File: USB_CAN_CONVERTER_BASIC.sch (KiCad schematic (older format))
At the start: 22 parts, among them P1 CONN_01X04, P2 CONN_01X02, P3 USB_A, P4 CONN_01X04, U1 STM32F042C6Ux, U2 PSD2CAN, U3 SN65HVD232D, U4 MCP1700T-3302E/TT, U5 USBLC6-2

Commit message: USB and CAN connector fix
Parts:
- P3: footprint Connect:USB_A -> usb_ccb_custom:USB_A_DS1097R
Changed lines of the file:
@@
 F 0 "P3" V 10823 4444 50  0000 L CNN
 F 1 "USB_A" V 10868 4444 50  0001 L CNN
-F 2 "Connect:USB_A" V 10750 4150 50  0001 C CNN
+F 2 "usb_ccb_custom:USB_A_DS1097R" V 10750 4150 50  0001 C CNN
 F 3 "" V 10750 4150 50  0000 C CNN
 	1    10800 4250

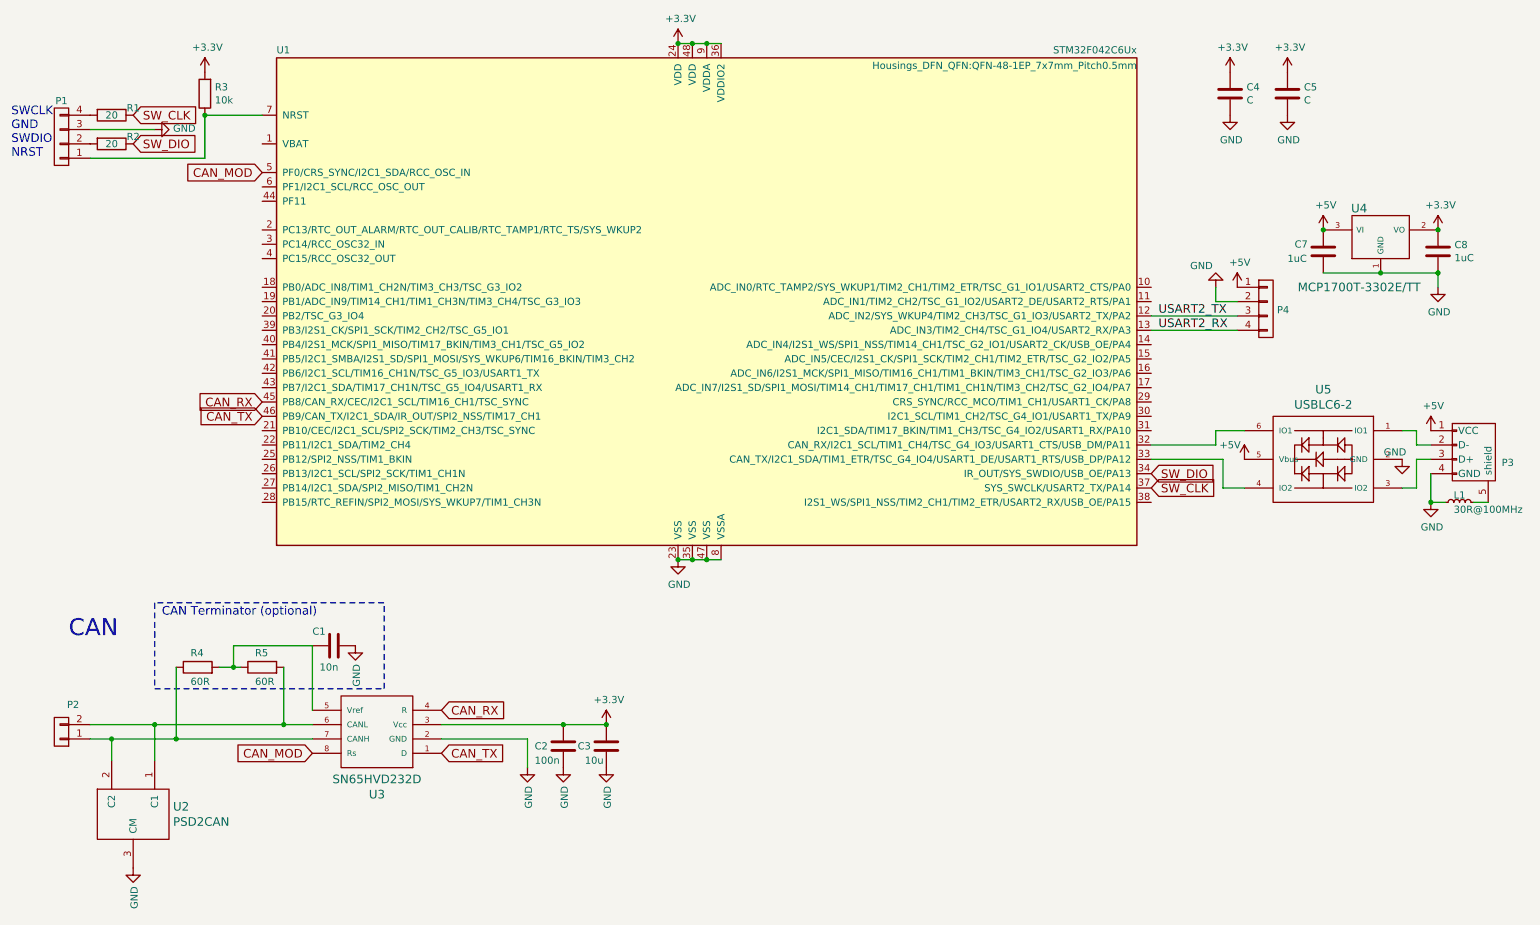
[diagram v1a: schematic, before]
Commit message: UART1 switch, logo creation, CAN footprint update, botom layer replacement.
UART1 switch, logo creation, CAN footprint update, botom layer
replacement.
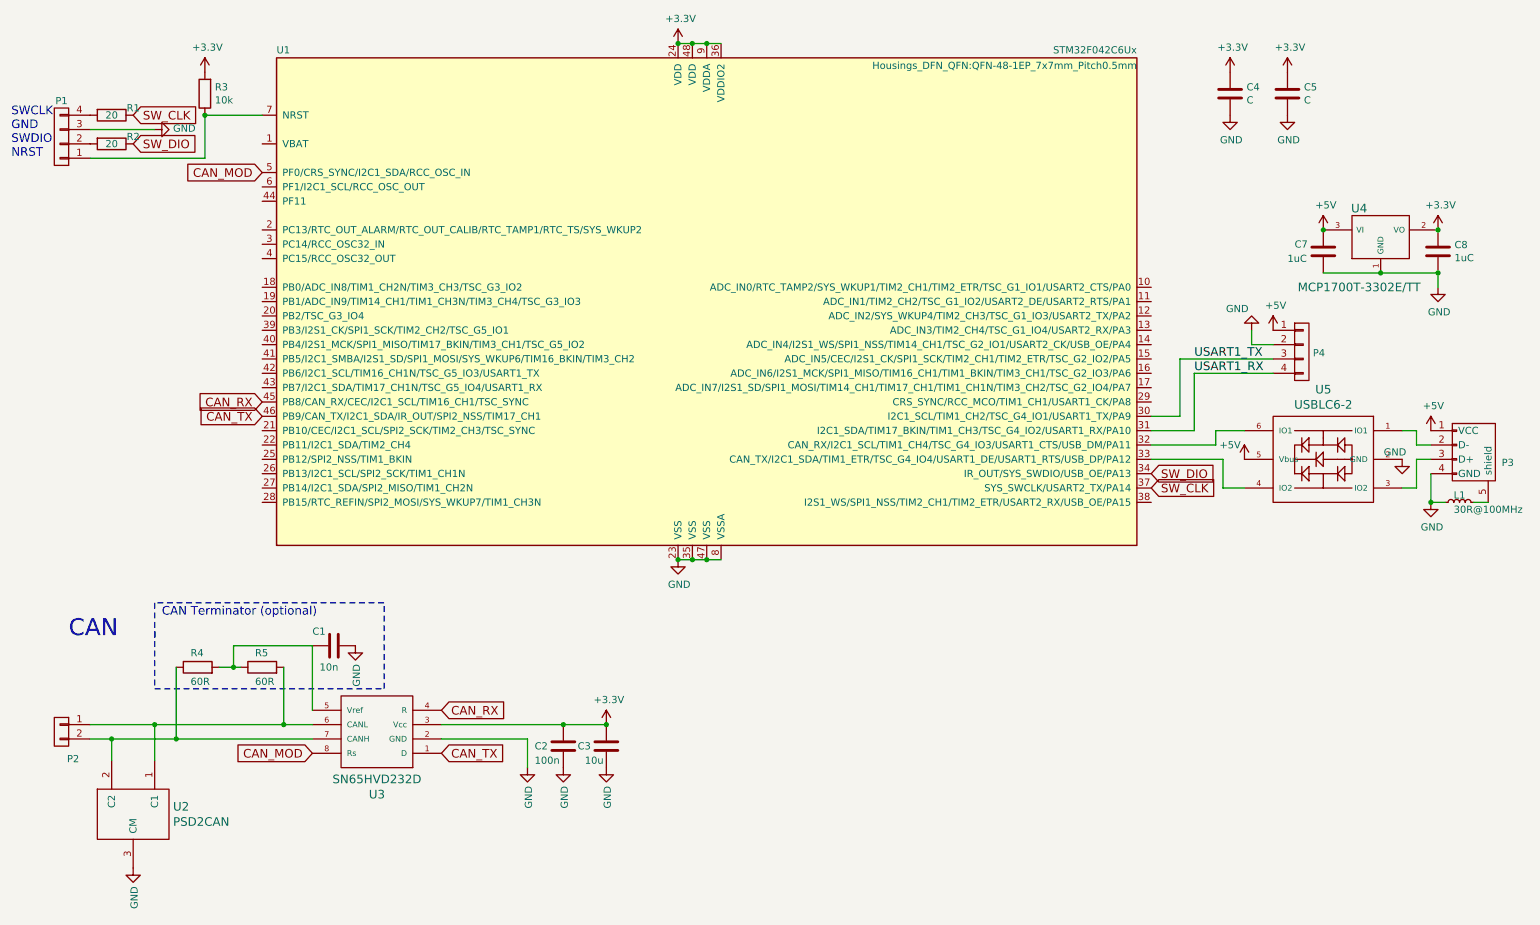
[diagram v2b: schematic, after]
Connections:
- net USART1_TX: now reaches U1.30 (I2C1_SCL/TIM1_CH2/TSC_G4_IO1/USART1_TX/PA9)
- net USART1_TX: now also P4.3 (P3)
- net USART1_RX: now reaches U1.31 (I2C1_SDA/TIM17_BKIN/TIM1_CH3/TSC_G4_IO2/USART1_RX/PA10)
- net USART1_RX: now also P4.4 (P4)
- net at R4.1, U2.2 (C2), U3.7 (CANH): now also P2.2 (P2); no longer P2.1 (P1)
- net at R5.2, U2.1 (C1), U3.6 (CANL): now also P2.1 (P1); no longer P2.2 (P2)
- net USART2_RX: no longer names the net of U1.13 (ADC_IN3/TIM2_CH4/TSC_G1_IO4/USART2_RX/PA3)
- net USART2_RX: no longer P4.4 (P4)
- net USART2_TX: no longer names the net of U1.12 (ADC_IN2/SYS_WKUP4/TIM2_CH3/TSC_G1_IO3/USART2_TX/PA2)
- net USART2_TX: no longer P4.3 (P3)
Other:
- moved on the sheet: P4
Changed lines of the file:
@@
 F 3 "" H 950 6150 50  0000 C CNN
 	1    950  6150
-	-1   0    0    1
+	-1   0    0    -1
 $EndComp
 $Comp
@@
 Wire Wire Line
 	10500 4550 10600 4550
-Wire Wire Line
-	8550 3250 9150 3250
-Wire Wire Line
-	8550 3350 9150 3350
 $Comp
 L GND #PWR022
 U 1 1 571ACD79
-P 9000 3050
-F 0 "#PWR022" H 9000 2800 50  0001 C CNN
-F 1 "GND" H 9100 2900 50  0000 C CNN
-F 2 "" H 9000 3050 50  0000 C CNN
-F 3 "" H 9000 3050 50  0000 C CNN
-	1    9000 3050
+P 9250 3350
+F 0 "#PWR022" H 9250 3100 50  0001 C CNN
+F 1 "GND" H 9350 3200 50  0000 C CNN
+F 2 "" H 9250 3350 50  0000 C CNN
+F 3 "" H 9250 3350 50  0000 C CNN
+	1    9250 3350
 	-1   0    0    1
 $EndComp
@@
 L CONN_01X04 P4
 U 1 1 571E76C6
-P 9350 3200
-F 0 "P4" H 9427 3192 50  0000 L CNN
-F 1 "CONN_01X04" H 9428 3147 50  0001 L CNN
-F 2 "Pin_Headers:Pin_Header_Angled_1x04" H 9427 3147 50  0001 L CNN
-F 3 "" H 9350 3200 50  0000 C CNN
-	1    9350 3200
+P 9600 3500
+F 0 "P4" H 9677 3492 50  0000 L CNN
+F 1 "CONN_01X04" H 9678 3447 50  0001 L CNN
+F 2 "Pin_Headers:Pin_Header_Angled_1x04" H 9677 3447 50  0001 L CNN
+F 3 "" H 9600 3500 50  0000 C CNN
+	1    9600 3500
 	1    0    0    -1
 $EndComp
@@
 L +5V #PWR023
 U 1 1 571E7816
-P 9150 3050
-F 0 "#PWR023" H 9150 2900 50  0001 C CNN
-F 1 "+5V" H 9168 3223 50  0000 C CNN
-F 2 "" H 9150 3050 50  0000 C CNN
-F 3 "" H 9150 3050 50  0000 C CNN
-	1    9150 3050
-	1    0    0    -1
-$EndComp
-Text Label 8600 3250 0    60   ~ 0
-USART2_TX
-Wire Wire Line
-	9000 3150 9150 3150
-Wire Wire Line
-	9000 3150 9000 3050
-Text Label 8600 3350 0    60   ~ 0
-USART2_RX
+P 9400 3350
+F 0 "#PWR023" H 9400 3200 50  0001 C CNN
+F 1 "+5V" H 9418 3523 50  0000 C CNN
+F 2 "" H 9400 3350 50  0000 C CNN
+F 3 "" H 9400 3350 50  0000 C CNN
+	1    9400 3350
+	1    0    0    -1
+$EndComp
+Text Label 8850 3550 0    60   ~ 0
+USART1_TX
+Wire Wire Line
+	9250 3450 9400 3450
+Wire Wire Line
+	9250 3450 9250 3350
+Text Label 8850 3650 0    60   ~ 0
+USART1_RX
 Connection ~ 1950 1850
+Wire Wire Line
+	8850 3650 9400 3650
+Wire Wire Line
+	8550 3950 8750 3950
+Wire Wire Line
+	8750 3950 8750 3550
+Wire Wire Line
+	8750 3550 9400 3550
+Wire Wire Line
+	8550 4050 8850 4050
+Wire Wire Line
+	8850 4050 8850 3650
 $EndSCHEMATC

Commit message: SWD connector update, logo generation,  board otline update.
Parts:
- removed P1: CONN_01X04, Pin_Headers:Pin_Header_Angled_1x04, symbol CONN_01X04
- removed R1, R2: 20, Resistors_SMD:R_0805, symbol R
- added P1: CONN_01X05, usb_ccb_custom:swd_smd_conn5, symbol CONN_01X05
- P4: footprint Pin_Headers:Pin_Header_Angled_1x04 -> usb_ccb_custom:Pin_Header_Angled_1x04m
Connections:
- net +3V3: now also P1.1 (P1)
- net GND: now also P1.4 (P4)
- net SW_CLK: now also P1.3 (P3)
- net SW_DIO: now also P1.5 (P5)
- net at R3.1, U1.7 (NRST): now also P1.2 (P2)
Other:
- note added: "SWCLK\nGND\nSWDIO\nNRST\nVTRG"
- note removed: "SWCLK\nGND\nSWDIO\nNRST"
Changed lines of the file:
@@
-$EndComp
-$Comp
-L CONN_01X04 P1
-U 1 1 570565AB
-P 950 2000
-F 0 "P1" H 950 1750 50  0000 C CNN
-F 1 "CONN_01X04" H 1050 1750 50  0001 C CNN
-F 2 "Pin_Headers:Pin_Header_Angled_1x04" H 950 2000 50  0001 C CNN
-F 3 "" H 950 2000 50  0000 C CNN
-	1    950  2000
-	-1   0    0    1
 $EndComp
 $Comp
@@
 	-1   0    0    1
 $EndComp
-$Comp
-L R R1
-U 1 1 5705681D
-P 1300 1850
-F 0 "R1" V 1250 2000 50  0000 C CNN
-F 1 "20" V 1300 1850 50  0000 C CNN
-F 2 "Resistors_SMD:R_0805" V 1230 1850 50  0001 C CNN
-F 3 "" H 1300 1850 50  0000 C CNN
-	1    1300 1850
-	0    1    1    0
-$EndComp
-$Comp
-L R R2
-U 1 1 570568EE
-P 1300 2050
-F 0 "R2" V 1250 2200 50  0000 C CNN
-F 1 "20" V 1300 2050 50  0000 C CNN
-F 2 "Resistors_SMD:R_0805" V 1230 2050 50  0001 C CNN
-F 3 "" H 1300 2050 50  0000 C CNN
-	1    1300 2050
-	0    1    1    0
-$EndComp
-Text Notes 600  2150 0    60   ~ 0
-SWCLK\nGND\nSWDIO\nNRST
+Text Notes 600  2300 0    60   ~ 0
+SWCLK\nGND\nSWDIO\nNRST\nVTRG
 $Comp
 L GND #PWR02
@@
 Text Notes 1650 5350 0    60   ~ 0
 CAN Terminator (optional)
-Text GLabel 1450 1850 2    60   Input ~ 0
+Text GLabel 1450 2050 2    60   Input ~ 0
 SW_CLK
 Text GLabel 8550 4450 2    60   Input ~ 0
 SW_CLK
-Text GLabel 1450 2050 2    60   Input ~ 0
+Text GLabel 1450 1850 2    60   Input ~ 0
 SW_DIO
 Text GLabel 8550 4350 2    60   Input ~ 0
@@
 F 0 "P4" H 9677 3492 50  0000 L CNN
 F 1 "CONN_01X04" H 9678 3447 50  0001 L CNN
-F 2 "Pin_Headers:Pin_Header_Angled_1x04" H 9677 3447 50  0001 L CNN
+F 2 "usb_ccb_custom:Pin_Header_Angled_1x04m" H 9677 3447 50  0001 L CNN
 F 3 "" H 9600 3500 50  0000 C CNN
 	1    9600 3500
@@
 Wire Wire Line
 	8850 4050 8850 3650
+$Comp
+L CONN_01X05 P1
+U 1 1 57800591
+P 950 2050
+F 0 "P1" H 869 1711 50  0000 C CNN
+F 1 "CONN_01X05" H 869 1710 50  0001 C CNN
+F 2 "usb_ccb_custom:swd_smd_conn5" H 869 1711 50  0001 C CNN
+F 3 "" H 950 2050 50  0000 C CNN
+	1    950  2050
+	-1   0    0    1
+$EndComp
+$Comp
+L +3.3V #PWR024
+U 1 1 57800AA2
+P 1150 2250
+F 0 "#PWR024" H 1150 2100 50  0001 C CNN
+F 1 "+3.3V" H 1168 2423 50  0000 C CNN
+F 2 "" H 1150 2250 50  0000 C CNN
+F 3 "" H 1150 2250 50  0000 C CNN
+	1    1150 2250
+	0    1    1    0
+$EndComp
+Wire Wire Line
+	1150 2050 1450 2050
+Wire Wire Line
+	1450 1850 1150 1850
+Connection ~ 2700 5550
 $EndSCHEMATC

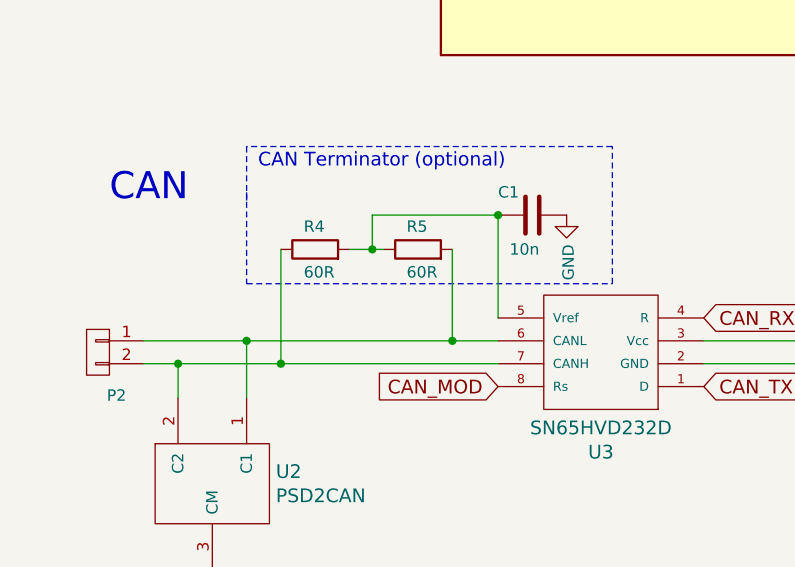
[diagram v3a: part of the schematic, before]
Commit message: CAN Jumpers addition
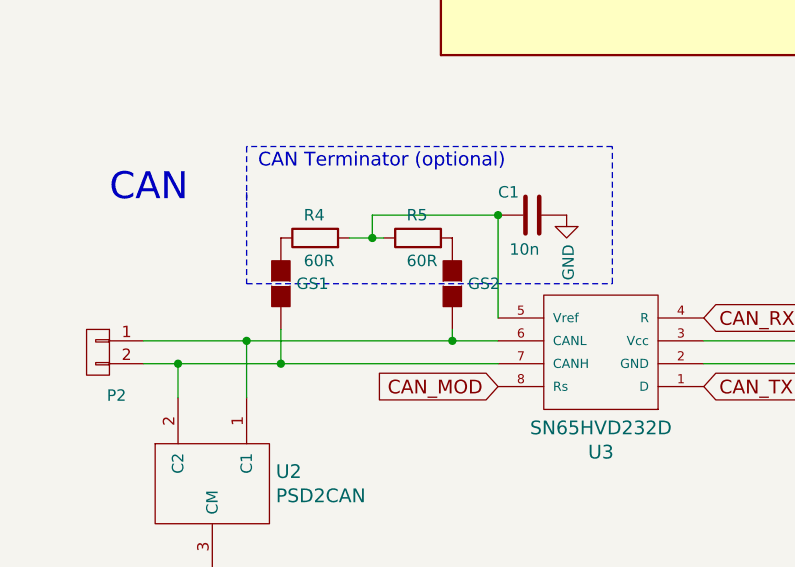
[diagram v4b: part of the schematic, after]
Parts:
- added GS1, GS2: GS2, Connect:GS2, symbol GS2
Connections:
- net at P2.1 (P1), U2.1 (C1), U3.6 (CANL): now also GS2.2 (G2); no longer R5.2
- net at P2.2 (P2), U2.2 (C2), U3.7 (CANH): now also GS1.2 (G2); no longer R4.1
- new net: GS1.1 (G1), R4.1
- new net: GS2.1 (G1), R5.2
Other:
- moved on the sheet: R4, R5
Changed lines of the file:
@@
 $EndComp
 $Comp
-L GND #PWR01
+L GND #PWR11
 U 1 1 570561B2
 P 5250 4950
-F 0 "#PWR01" H 5250 4700 50  0001 C CNN
+F 0 "#PWR11" H 5250 4700 50  0001 C CNN
 F 1 "GND" H 5258 4777 50  0000 C CNN
 F 2 "" H 5250 4950 50  0000 C CNN
@@
 SWCLK\nGND\nSWDIO\nNRST\nVTRG
 $Comp
-L GND #PWR02
+L GND #PWR3
 U 1 1 57056C83
 P 1600 1950
-F 0 "#PWR02" H 1600 1700 50  0001 C CNN
+F 0 "#PWR3" H 1600 1700 50  0001 C CNN
 F 1 "GND" V 1608 1822 50  0000 R CNN
 F 2 "" H 1600 1950 50  0000 C CNN
@@
 $EndComp
 $Comp
-L GND #PWR03
+L GND #PWR22
 U 1 1 5706C070
 P 10500 4550
-F 0 "#PWR03" H 10500 4300 50  0001 C CNN
+F 0 "#PWR22" H 10500 4300 50  0001 C CNN
 F 1 "GND" H 10508 4377 50  0000 C CNN
 F 2 "" H 10500 4550 50  0000 C CNN
@@
 $EndComp
 $Comp
-L +5V #PWR04
+L +5V #PWR21
 U 1 1 5706C74A
 P 10500 4050
-F 0 "#PWR04" H 10500 3900 50  0001 C CNN
+F 0 "#PWR21" H 10500 3900 50  0001 C CNN
 F 1 "+5V" H 10518 4223 50  0000 C CNN
 F 2 "" H 10500 4050 50  0000 C CNN
@@
 $EndComp
 $Comp
-L +5V #PWR05
+L +5V #PWR19
 U 1 1 5706E498
 P 9750 2650
-F 0 "#PWR05" H 9750 2500 50  0001 C CNN
+F 0 "#PWR19" H 9750 2500 50  0001 C CNN
 F 1 "+5V" H 9768 2823 50  0000 C CNN
 F 2 "" H 9750 2650 50  0000 C CNN
@@
 $EndComp
 $Comp
-L +3.3V #PWR06
+L +3.3V #PWR4
 U 1 1 5706E500
 P 1950 1550
-F 0 "#PWR06" H 1950 1400 50  0001 C CNN
+F 0 "#PWR4" H 1950 1400 50  0001 C CNN
 F 1 "+3.3V" H 1968 1723 50  0000 C CNN
 F 2 "" H 1950 1550 50  0000 C CNN
@@
 $EndComp
 $Comp
-L +3.3V #PWR07
+L +3.3V #PWR10
 U 1 1 5706E57B
 P 5250 1350
-F 0 "#PWR07" H 5250 1200 50  0001 C CNN
+F 0 "#PWR10" H 5250 1200 50  0001 C CNN
 F 1 "+3.3V" H 5268 1523 50  0000 C CNN
 F 2 "" H 5250 1350 50  0000 C CNN
@@
 $EndComp
 $Comp
-L +3.3V #PWR08
+L +3.3V #PWR23
 U 1 1 5706E6F4
 P 10550 2650
-F 0 "#PWR08" H 10550 2500 50  0001 C CNN
+F 0 "#PWR23" H 10550 2500 50  0001 C CNN
 F 1 "+3.3V" H 10568 2823 50  0000 C CNN
 F 2 "" H 10550 2650 50  0000 C CNN
@@
 $EndComp
 $Comp
-L GND #PWR09
+L GND #PWR13
 U 1 1 5706EDB2
 P 9100 1850
-F 0 "#PWR09" H 9100 1600 50  0001 C CNN
+F 0 "#PWR13" H 9100 1600 50  0001 C CNN
 F 1 "GND" H 9108 1677 50  0000 C CNN
 F 2 "" H 9100 1850 50  0000 C CNN
@@
 $EndComp
 $Comp
-L GND #PWR010
+L GND #PWR18
 U 1 1 5706EDDA
 P 9500 1850
-F 0 "#PWR010" H 9500 1600 50  0001 C CNN
+F 0 "#PWR18" H 9500 1600 50  0001 C CNN
 F 1 "GND" H 9508 1677 50  0000 C CNN
 F 2 "" H 9500 1850 50  0000 C CNN
@@
 $EndComp
 $Comp
-L +3.3V #PWR011
+L +3.3V #PWR17
 U 1 1 5706EE52
 P 9500 1550
-F 0 "#PWR011" H 9500 1400 50  0001 C CNN
+F 0 "#PWR17" H 9500 1400 50  0001 C CNN
 F 1 "+3.3V" H 9518 1723 50  0000 C CNN
 F 2 "" H 9500 1550 50  0000 C CNN
@@
 $EndComp
 $Comp
-L +3.3V #PWR012
+L +3.3V #PWR12
 U 1 1 5706EEDE
 P 9100 1550
-F 0 "#PWR012" H 9100 1400 50  0001 C CNN
+F 0 "#PWR12" H 9100 1400 50  0001 C CNN
 F 1 "+3.3V" H 9118 1723 50  0000 C CNN
 F 2 "" H 9100 1550 50  0000 C CNN
@@
 $EndComp
 $Comp
-L GND #PWR013
+L GND #PWR24
 U 1 1 5706F734
 P 10550 3050
-F 0 "#PWR013" H 10550 2800 50  0001 C CNN
+F 0 "#PWR24" H 10550 2800 50  0001 C CNN
 F 1 "GND" H 10558 2877 50  0000 C CNN
 F 2 "" H 10550 3050 50  0000 C CNN
@@
 $EndComp
 $Comp
-L +3.3V #PWR014
+L +3.3V #PWR8
 U 1 1 5708A6C5
 P 4750 6100
-F 0 "#PWR014" H 4750 5950 50  0001 C CNN
+F 0 "#PWR8" H 4750 5950 50  0001 C CNN
 F 1 "+3.3V" H 4768 6273 50  0000 C CNN
 F 2 "" H 4750 6100 50  0000 C CNN
@@
 $EndComp
 $Comp
-L GND #PWR015
+L GND #PWR9
 U 1 1 5708A9FB
 P 4750 6400
-F 0 "#PWR015" H 4750 6150 50  0001 C CNN
+F 0 "#PWR9" H 4750 6150 50  0001 C CNN
 F 1 "GND" V 4758 6272 50  0000 R CNN
 F 2 "" H 4750 6400 50  0000 C CNN
@@
 $EndComp
 $Comp
-L GND #PWR016
+L GND #PWR7
 U 1 1 5708B621
 P 4450 6400
-F 0 "#PWR016" H 4450 6150 50  0001 C CNN
+F 0 "#PWR7" H 4450 6150 50  0001 C CNN
 F 1 "GND" V 4458 6272 50  0000 R CNN
 F 2 "" H 4450 6400 50  0000 C CNN
@@
 $EndComp
 $Comp
-L GND #PWR017
+L GND #PWR6
 U 1 1 5708BDA5
 P 4200 6400
-F 0 "#PWR017" H 4200 6150 50  0001 C CNN
+F 0 "#PWR6" H 4200 6150 50  0001 C CNN
 F 1 "GND" V 4208 6272 50  0000 R CNN
 F 2 "" H 4200 6400 50  0000 C CNN
@@
 $EndComp
 $Comp
-L GND #PWR018
+L GND #PWR2
 U 1 1 5708D67B
 P 1450 7100
-F 0 "#PWR018" H 1450 6850 50  0001 C CNN
+F 0 "#PWR2" H 1450 6850 50  0001 C CNN
 F 1 "GND" V 1458 6972 50  0000 R CNN
 F 2 "" H 1450 7100 50  0000 C CNN
@@
 L R R4
 U 1 1 5708DAC6
-P 1900 5700
-F 0 "R4" V 2000 5750 50  0000 R CNN
-F 1 "60R" V 1800 5750 50  0000 R CNN
-F 2 "Resistors_SMD:R_0805" H 1830 5791 50  0001 R CNN
-F 3 "" H 1900 5700 50  0000 C CNN
-	1    1900 5700
+P 1900 5650
+F 0 "R4" V 2000 5700 50  0000 R CNN
+F 1 "60R" V 1800 5700 50  0000 R CNN
+F 2 "Resistors_SMD:R_0805" H 1830 5741 50  0001 R CNN
+F 3 "" H 1900 5650 50  0000 C CNN
+	1    1900 5650
 	0    -1   -1   0
 $EndComp
@@
 L R R5
 U 1 1 5708DE1C
-P 2350 5700
-F 0 "R5" V 2450 5750 50  0000 R CNN
-F 1 "60R" V 2250 5750 50  0000 R CNN
-F 2 "Resistors_SMD:R_0805" H 2280 5791 50  0001 R CNN
-F 3 "" H 2350 5700 50  0000 C CNN
-	1    2350 5700
+P 2350 5650
+F 0 "R5" V 2450 5700 50  0000 R CNN
+F 1 "60R" V 2250 5700 50  0000 R CNN
+F 2 "Resistors_SMD:R_0805" H 2280 5741 50  0001 R CNN
+F 3 "" H 2350 5650 50  0000 C CNN
+	1    2350 5650
 	0    -1   -1   0
 $EndComp
@@
 $EndComp
 $Comp
-L GND #PWR019
+L GND #PWR5
 U 1 1 5708E325
 P 3000 5550
-F 0 "#PWR019" H 3000 5300 50  0001 C CNN
+F 0 "#PWR5" H 3000 5300 50  0001 C CNN
 F 1 "GND" V 3008 5422 50  0000 R CNN
 F 2 "" H 3000 5550 50  0000 C CNN
@@
 $EndComp
 $Comp
-L +5V #PWR020
+L +5V #PWR14
 U 1 1 5716787A
 P 9200 4250
-F 0 "#PWR020" H 9200 4100 50  0001 C CNN
+F 0 "#PWR14" H 9200 4100 50  0001 C CNN
 F 1 "+5V" H 9100 4350 50  0000 C CNN
 F 2 "" H 9200 4250 50  0000 C CNN
@@
 $EndComp
 $Comp
-L GND #PWR021
+L GND #PWR20
 U 1 1 57167911
 P 10300 4250
-F 0 "#PWR021" H 10300 4000 50  0001 C CNN
+F 0 "#PWR20" H 10300 4000 50  0001 C CNN
 F 1 "GND" H 10250 4300 50  0000 C CNN
 F 2 "" H 10300 4250 50  0000 C CNN
@@
 Connection ~ 1600 6100
 Connection ~ 1300 6200
-Wire Wire Line
-	2200 5700 2050 5700
-Wire Wire Line
-	2500 5700 2500 6100
 Connection ~ 2500 6100
-Wire Wire Line
-	1750 5700 1750 6200
 Connection ~ 1750 6200
 Wire Wire Line
-	2150 5700 2150 5550
-Wire Wire Line
 	2150 5550 2700 5550
 Wire Wire Line
 	2700 5550 2700 6000
-Connection ~ 2150 5700
+Connection ~ 2150 5650
 Wire Notes Line
 	1600 5450 1600 5850
@@
 	10500 4550 10600 4550
 $Comp
-L GND #PWR022
+L GND #PWR15
 U 1 1 571ACD79
 P 9250 3350
-F 0 "#PWR022" H 9250 3100 50  0001 C CNN
+F 0 "#PWR15" H 9250 3100 50  0001 C CNN
 F 1 "GND" H 9350 3200 50  0000 C CNN
 F 2 "" H 9250 3350 50  0000 C CNN
@@
 $EndComp
 $Comp
-L +5V #PWR023
+L +5V #PWR16
 U 1 1 571E7816
 P 9400 3350
-F 0 "#PWR023" H 9400 3200 50  0001 C CNN
+F 0 "#PWR16" H 9400 3200 50  0001 C CNN
 F 1 "+5V" H 9418 3523 50  0000 C CNN
 F 2 "" H 9400 3350 50  0000 C CNN
@@
 $EndComp
 $Comp
-L +3.3V #PWR024
+L +3.3V #PWR1
 U 1 1 57800AA2
 P 1150 2250
-F 0 "#PWR024" H 1150 2100 50  0001 C CNN
+F 0 "#PWR1" H 1150 2100 50  0001 C CNN
 F 1 "+3.3V" H 1168 2423 50  0000 C CNN
 F 2 "" H 1150 2250 50  0000 C CNN
@@
 	1450 1850 1150 1850
 Connection ~ 2700 5550
+$Comp
+L GS2 GS1
+U 1 1 5781392F
+P 1750 5850
+F 0 "GS1" H 1818 5850 50  0000 L CNN
+F 1 "GS2" H 1818 5850 50  0001 L CNN
+F 2 "Connect:GS2" H 1818 5805 50  0001 L CNN
+F 3 "" H 1750 5850 50  0000 C CNN
+	1    1750 5850
+	1    0    0    -1
+$EndComp
+Wire Wire Line
+	2150 5550 2150 5650
+Wire Wire Line
+	2050 5650 2200 5650
+Wire Wire Line
+	1750 6050 1750 6200
+$Comp
+L GS2 GS2
+U 1 1 57813F91
+P 2500 5850
+F 0 "GS2" H 2568 5850 50  0000 L CNN
+F 1 "GS2" H 2568 5850 50  0001 L CNN
+F 2 "Connect:GS2" H 2568 5805 50  0001 L CNN
+F 3 "" H 2500 5850 50  0000 C CNN
+	1    2500 5850
+	1    0    0    -1
+$EndComp
+Wire Wire Line
+	2500 6050 2500 6100
 $EndSCHEMATC
